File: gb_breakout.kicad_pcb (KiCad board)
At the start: 2 copper layers, 51 x 60.7 mm, 13 parts, among them J1 Conn_02x16_Counter_Clockwise, U1 Cartridge_Bus

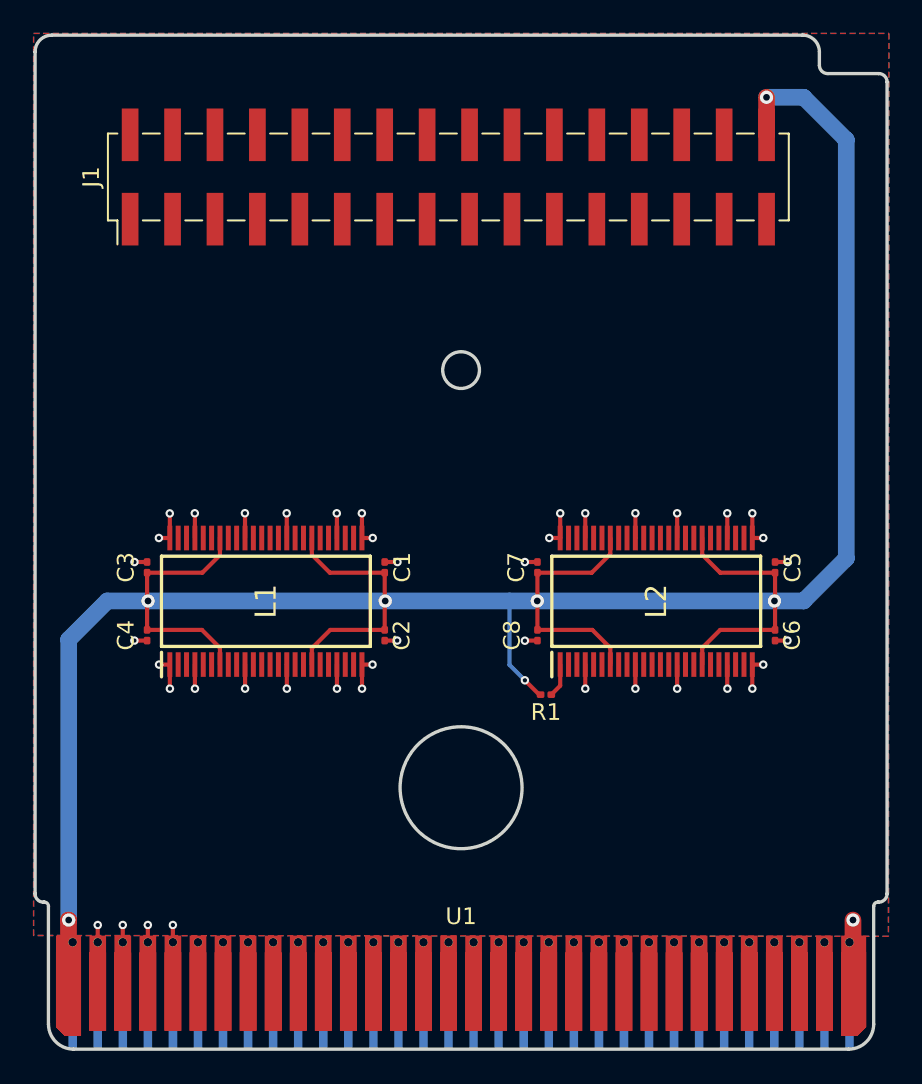
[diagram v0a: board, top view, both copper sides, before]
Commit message: begin routing address lines
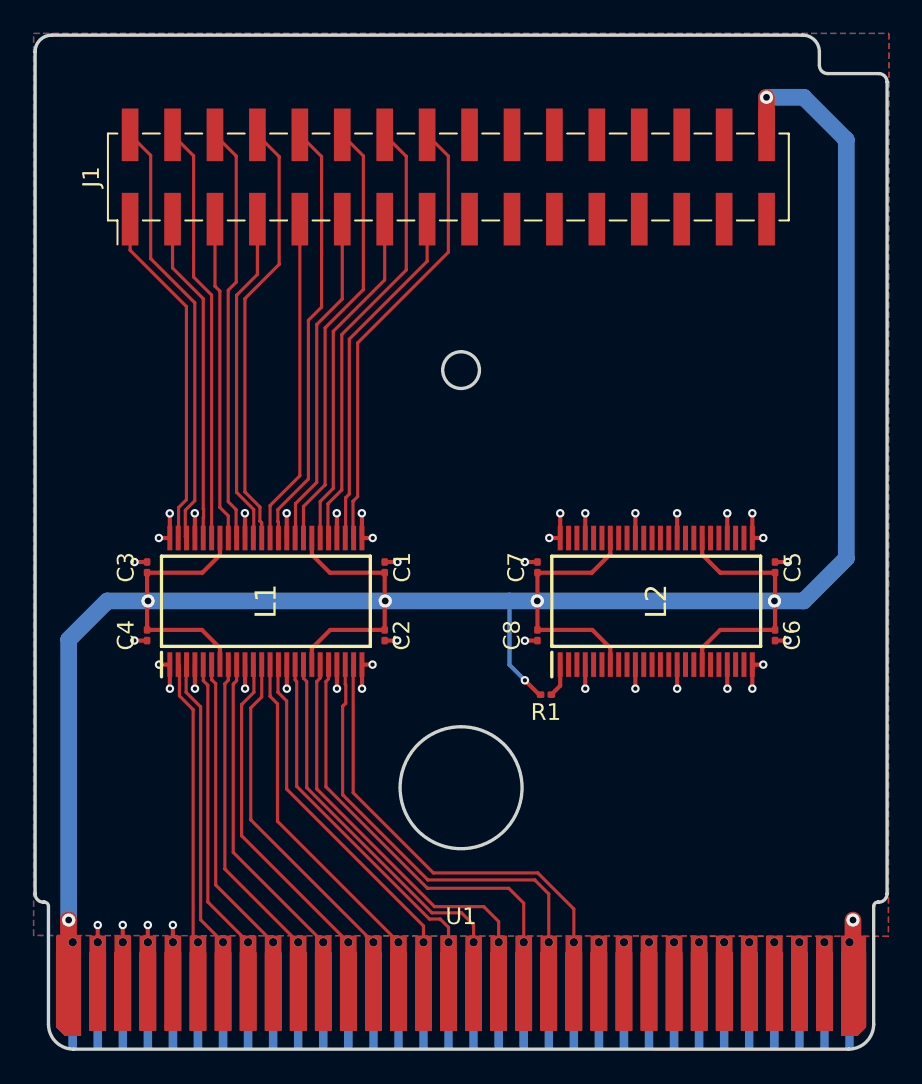
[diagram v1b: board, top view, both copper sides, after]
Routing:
- net BO_A15: track 0.00 -> 27.0 mm
- net BO_A13: track 0.00 -> 26.6 mm
- net BO_A11: track 0.00 -> 26.1 mm
- net BO_A1: track 0.00 -> 26.0 mm
- net BO_A7: track 0.00 -> 25.9 mm
- net BO_A9: track 0.00 -> 25.8 mm
- net GB_A15: track 0.00 -> 25.8 mm
- net GB_A14: track 0.00 -> 25.6 mm
- net BO_A3: track 0.00 -> 25.1 mm
- net BO_A5: track 0.00 -> 25.1 mm
- net GB_A13: track 0.00 -> 24.4 mm
- net GB_A12: track 0.00 -> 22.9 mm
- net GB_A11: track 0.00 -> 21.9 mm
- net BO_A14: track 0.00 -> 21.1 mm
- net GB_A10: track 0.00 -> 20.8 mm
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
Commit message: switched to 74ALVC164245 for level shifting
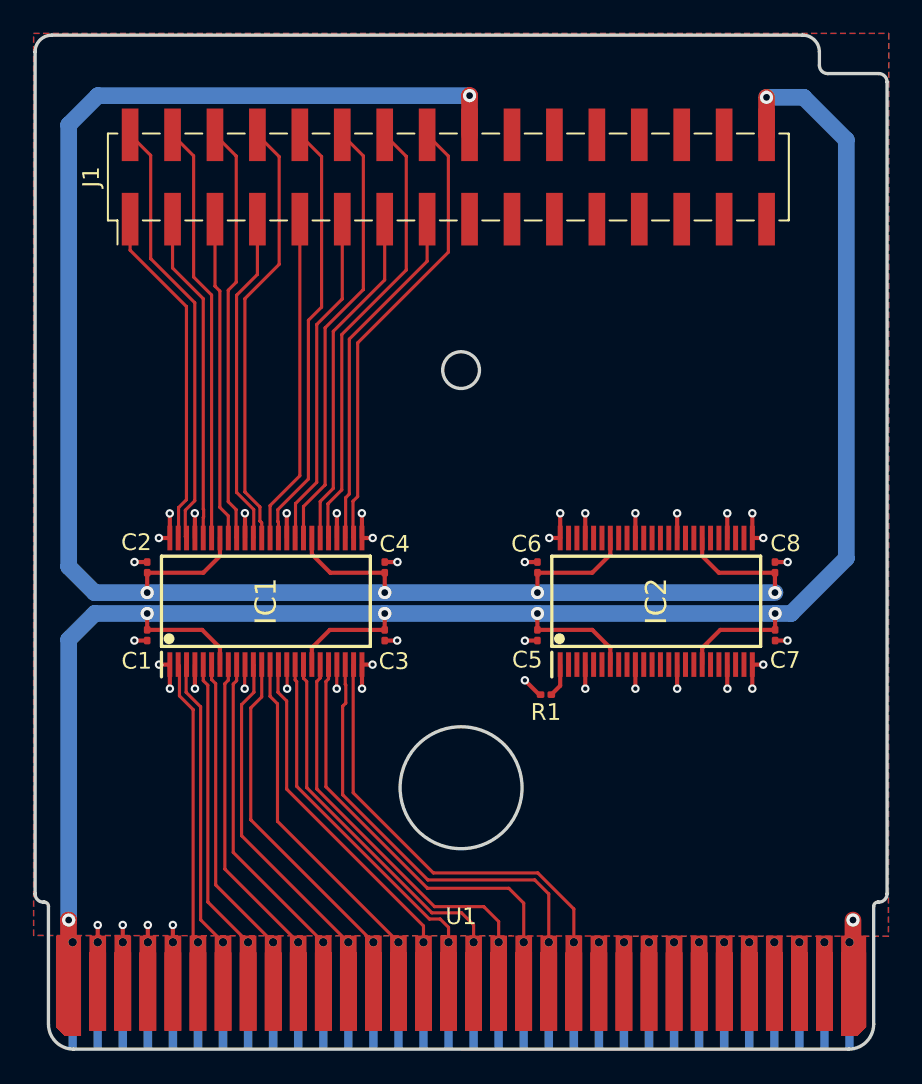
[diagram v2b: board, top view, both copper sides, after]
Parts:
- removed L1, L2: 74ACT16245DGGR, 74ACT16245DGGR:SOP50P810X120-48N
- added IC1: 74ALVC164245DGG_11, 74ALVC164245DGG_11:SOP50P810X120-48N, F.Cu at (130.6, 96.5)
- added IC2: 74ALVC164245DGG_11, 74ALVC164245DGG_11:SOP50P810X120-48N, F.Cu at (153.9, 96.5)
- moved C7 37.6 mm to (161.0, 98.5)
- moved C2 37.6 mm to (123.5, 94.5)
- moved C4 23.7 mm to (137.7, 94.5), turned to -90 degrees
- moved C5 23.7 mm to (146.8, 98.5), turned to 90 degrees
- moved C1 14.8 mm to (123.5, 98.5), turned to 90 degrees
- moved C8 14.8 mm to (161.0, 94.5), turned to -90 degrees
- renumbered C5 to C2, C2 to C3, C6 to C4, C3 to C5, C7 to C6, C4 to C7
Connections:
- C2 pad 2: +5V -> +3V3
- C4 pad 2: +5V -> +3V3
- C6 pad 2: +5V -> +3V3
- C8 pad 2: +5V -> +3V3
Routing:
- net +3V3: track 0.00 -> 124.5 mm, vias 0 -> 5
- net +5V: track 166.6 -> 128.4 mm

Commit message: finish routing address lines, start routing data lines
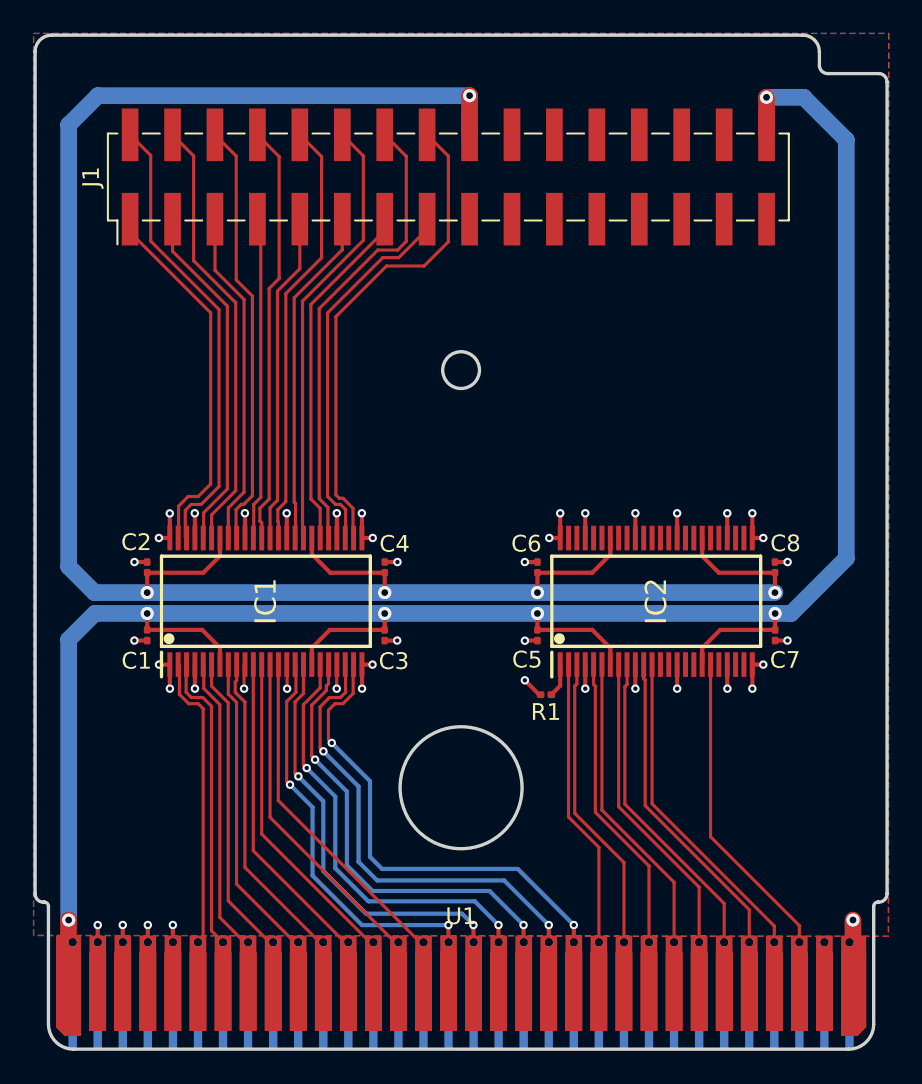
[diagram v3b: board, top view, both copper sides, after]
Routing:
- net GB_D7: track 0.00 -> 19.7 mm
- net GB_D6: track 0.00 -> 19.2 mm
- net GB_D5: track 0.00 -> 19.1 mm
- net GB_~{RST}: track 0.00 -> 18.8 mm
- net GB_D4: track 0.00 -> 18.6 mm
- net GB_D3: track 0.00 -> 18.4 mm
- net GB_D2: track 0.00 -> 18.0 mm
- net GB_D1: track 0.00 -> 17.9 mm
- net GB_D0: track 0.00 -> 17.4 mm
- net GB_A10: track 20.8 -> 24.1 mm, vias 0 -> 2
- net GB_A11: track 21.9 -> 24.6 mm, vias 0 -> 2
- net GB_A12: track 22.9 -> 25.6 mm, vias 0 -> 2
- net GB_A15: track 25.8 -> 28.4 mm, vias 0 -> 2
- net BO_A15: track 27.0 -> 29.3 mm
- net GB_A14: track 25.6 -> 27.8 mm, vias 0 -> 2
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
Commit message: switch decoupling caps to imperial 0603
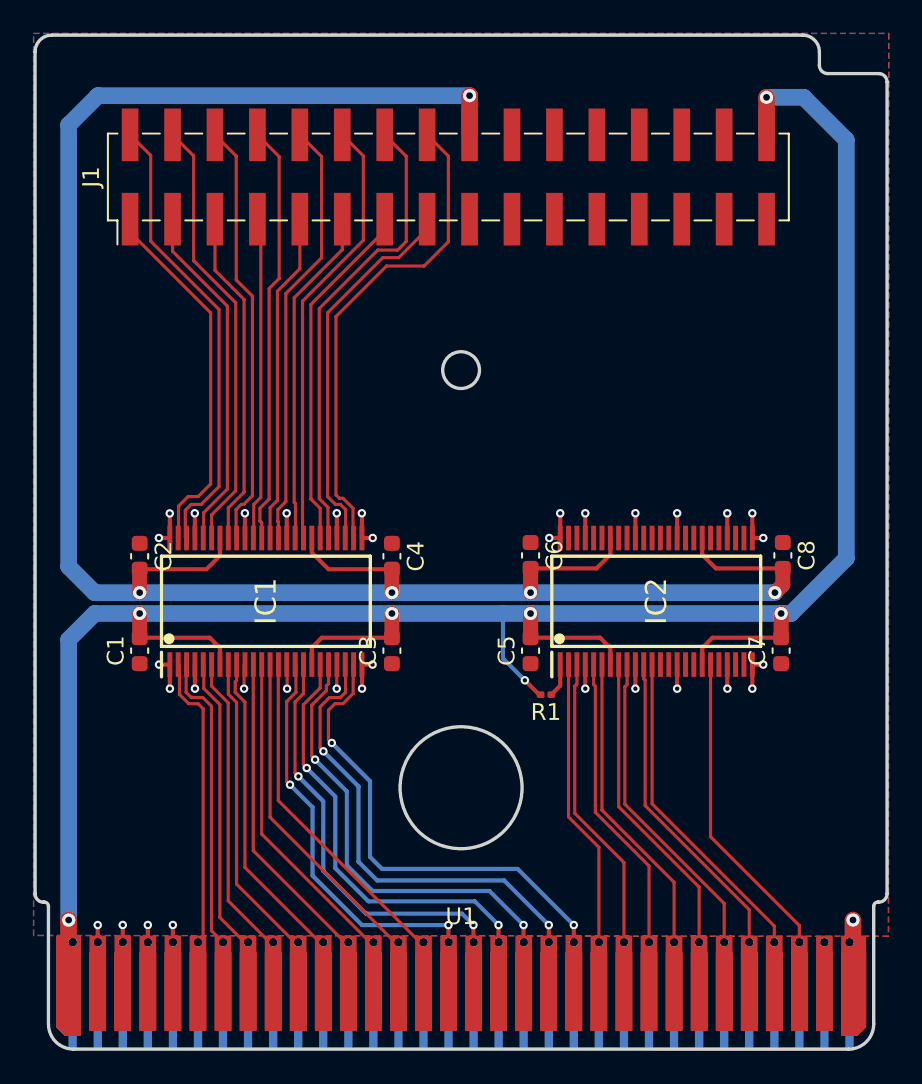
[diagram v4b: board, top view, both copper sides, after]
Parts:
- C1, C2, C3, C4, C5, C6, C7, C8: footprint Capacitor_SMD:C_0201_0603Metric -> Capacitor_SMD:C_0603_1608Metric
- moved C1 1.03 mm to (123.0, 99.5)
- moved C3 1.02 mm to (138.1, 99.5)
- moved C5 1.01 mm to (146.4, 99.5)
- moved C7 0.99 mm to (161.4, 99.5)
- moved C8 0.86 mm to (161.5, 93.8)
- moved C6 0.83 mm to (146.4, 93.8)
- moved C2 0.80 mm to (123.0, 93.8)
- moved C4 0.79 mm to (138.1, 93.8)
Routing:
- net +5V: track 128.4 -> 135.6 mm
- net GND: track 45.9 -> 39.8 mm, vias 39 -> 31
- net +3V3: track 124.5 -> 126.9 mm

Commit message: finish cart edge routing to bus transcievers
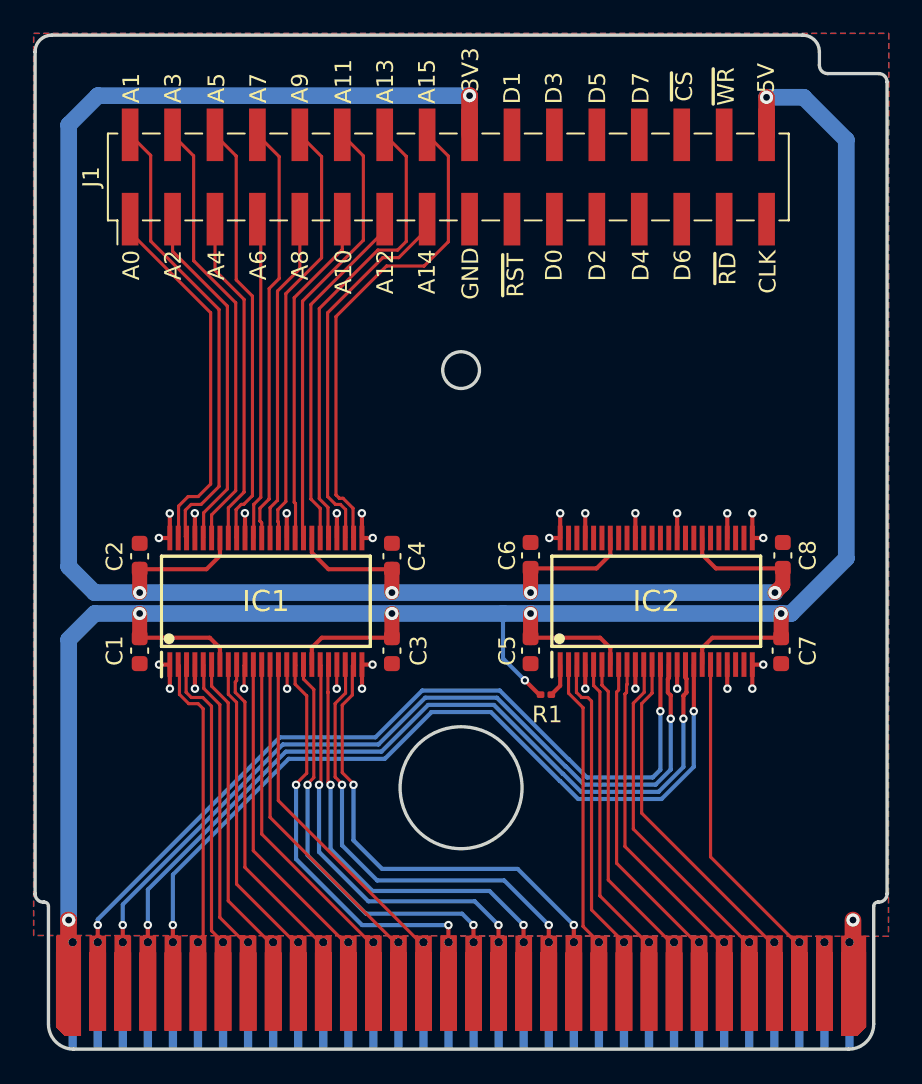
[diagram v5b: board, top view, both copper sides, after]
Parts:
- added G***: LOGO, oshw_silk:oshw_silk, F.Cu at (129.7, 80.1)
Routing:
- net GB_CLK: track 1.03 -> 49.4 mm, vias 1 -> 2
- net GB_~{WR}: track 3.05 -> 51.1 mm, vias 1 -> 2
- net GB_~{RD}: track 1.03 -> 48.8 mm, vias 1 -> 2
- net GB_~{CS}: track 1.03 -> 48.3 mm, vias 1 -> 2
- net GB_A14: track 27.8 -> 26.6 mm
- net GB_A15: track 28.4 -> 27.4 mm
- net GB_A13: track 26.4 -> 25.6 mm
- net GB_A12: track 25.6 -> 24.9 mm
- net GB_D7: track 19.7 -> 20.3 mm
- net GB_D6: track 19.2 -> 19.9 mm
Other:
- board text added: "3V3"
- board text added: "5V"
- board text added: "A0"
- board text added: "A1"
- board text added: "A10"
- board text added: "A11"
- board text added: "A12"
- board text added: "A13"
- board text added: "A14"
- board text added: "A15"
- board text added: "A2"
- board text added: "A3"
- board text added: "A4"
- board text added: "A5"
- board text added: "A6"
- board text added: "A7"
- board text added: "A8"
- board text added: "A9"
- board text added: "CLK"
- board text added: "D0"
- board text added: "D1"
- board text added: "D2"
- board text added: "D3"
- board text added: "D4"
- board text added: "D5"
- board text added: "D6"
- board text added: "D7"
- board text added: "GB-BREAKOUT"
- board text added: "GND"
- board text added: "github.com/Y2K-x"
- board text added: "~{CS}"
- board text added: "~{RD}"
- board text added: "~{RST}"
- board text added: "~{WR}"

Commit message: fix pin header pinout to make better sense to route
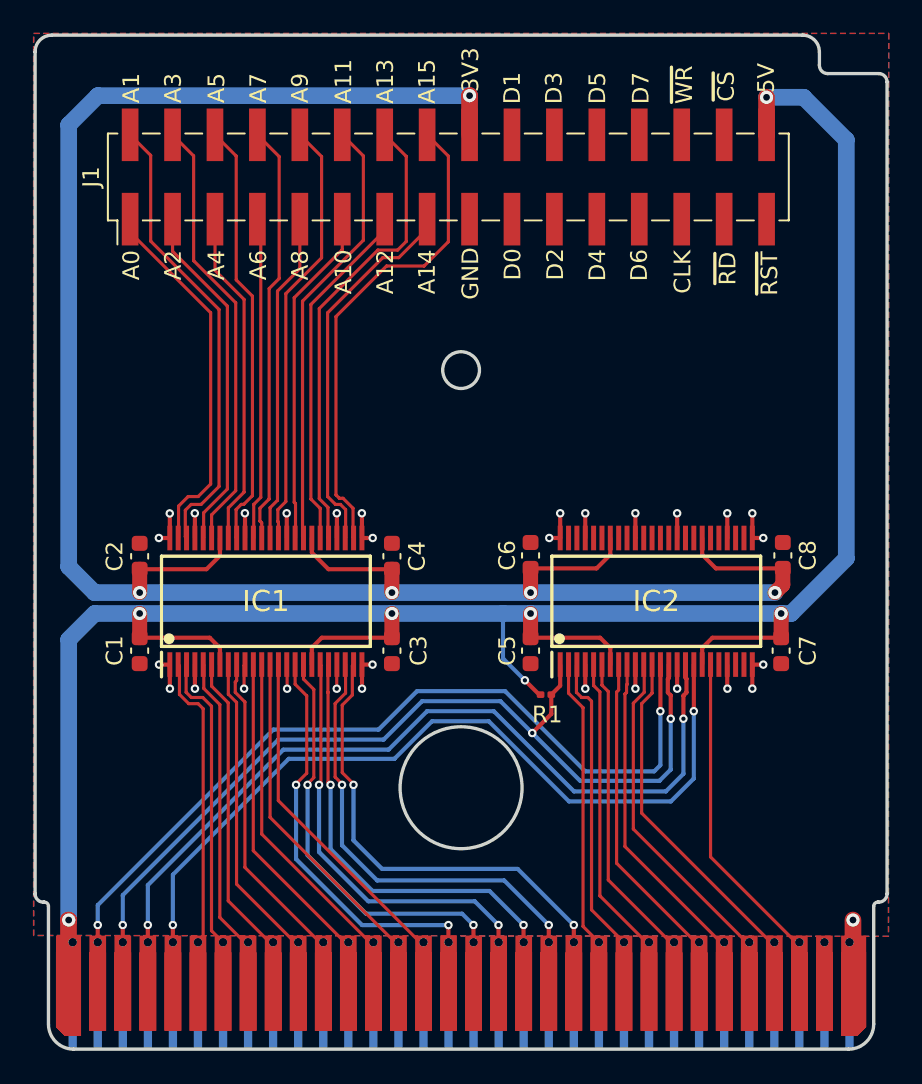
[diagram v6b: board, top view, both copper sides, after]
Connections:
- J1 pad 19: BO_~{RST} -> BO_D0
- J1 pad 20: BO_D7 -> BO_D1
- J1 pad 21: BO_D6 -> BO_D2
- J1 pad 22: BO_D5 -> BO_D3
- J1 pad 24: BO_D3 -> BO_D5
- J1 pad 25: BO_D2 -> BO_D6
- J1 pad 26: BO_D1 -> BO_D7
- J1 pad 27: BO_D0 -> BO_CLK
- J1 pad 28: BO_~{CS} -> BO_~{WR}
- J1 pad 30: BO_~{WR} -> BO_~{CS}
- J1 pad 31: BO_CLK -> BO_~{RST}
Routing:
- net GB_~{WR}: track 51.1 -> 53.9 mm, vias 2 -> 3

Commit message: PCB done
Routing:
- net BO_D1: track 0.00 -> 26.8 mm
- net BO_~{CS}: track 0.00 -> 26.6 mm
- net BO_D3: track 0.00 -> 25.9 mm
- net BO_~{WR}: track 0.00 -> 25.8 mm
- net BO_D7: track 0.00 -> 25.1 mm
- net BO_D5: track 0.00 -> 25.1 mm
- net BO_~{RST}: track 0.00 -> 21.5 mm
- net BO_D0: track 0.00 -> 21.5 mm
- net BO_~{RD}: track 0.00 -> 20.8 mm
- net BO_D2: track 0.00 -> 20.7 mm
- net BO_CLK: track 0.00 -> 19.8 mm
- net BO_D4: track 0.00 -> 19.8 mm
- net BO_D6: track 0.00 -> 19.2 mm
- net GND: vias 31 -> 105
